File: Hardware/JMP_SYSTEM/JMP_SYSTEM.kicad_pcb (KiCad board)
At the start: 2 copper layers, 211.7 x 145 mm, 72 parts, among them J1 BLUEPILL, J10 Debug, J11 Debug, J12 RELE, J13 Port_access, J14 Port_access, J15 Port_access, J16 Port_access, J17 Port_access, J18 Port_access, J19 Port_access, J2 Debug, J20 Port_access, J21 Port_access, J22 Debug, J3 Debug, J4 BLUETOOTH, J5 MODULO SD, J6 Debug, J7 Debug, J8 Port_access, J9 Debug, SW1 SENSOR, SW10 BT_RST, SW2 SENSOR, SW3 BT_LEFT, SW4 BT_RIGHT, SW5 BT_UP, SW6 BT_DOWN, SW7 BT_STOP, SW8 BT_MENU, SW9 BT_OK, U1 LCD-PCF8574, U2 LCD-5LC02, U3 TP4056_MODULE, U4 Modulo_DC-DC_Boost_XL6009

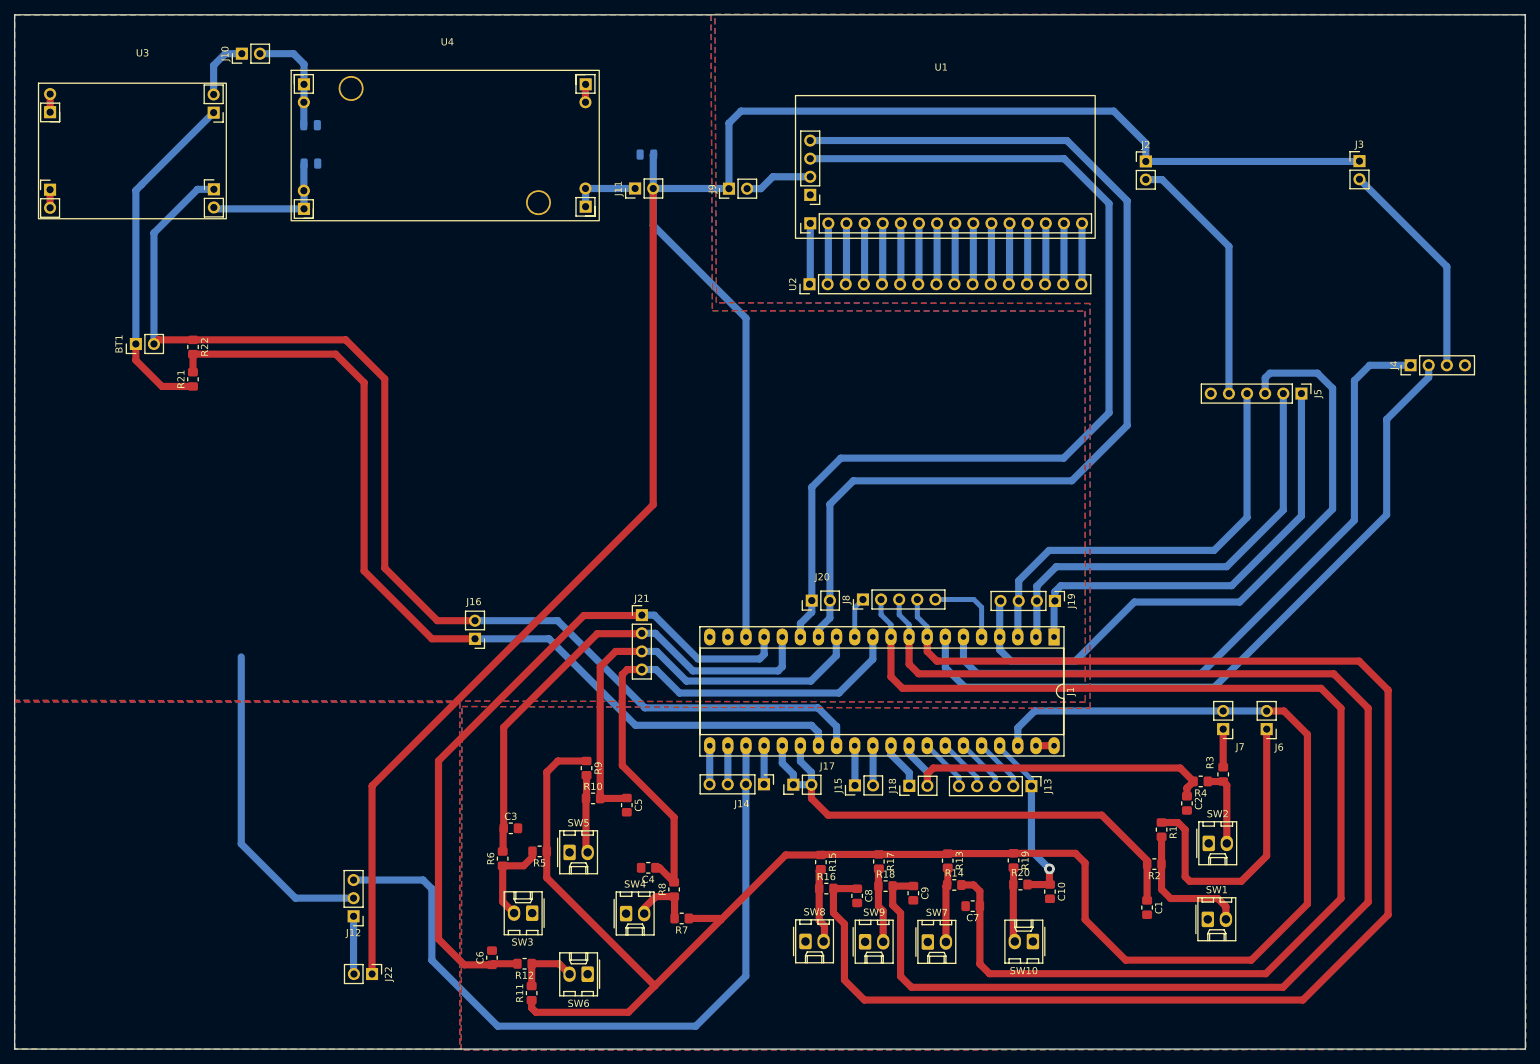
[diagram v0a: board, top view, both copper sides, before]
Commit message: Separacao do projeto em 3 PCBs - Core, PowerSupply, Display
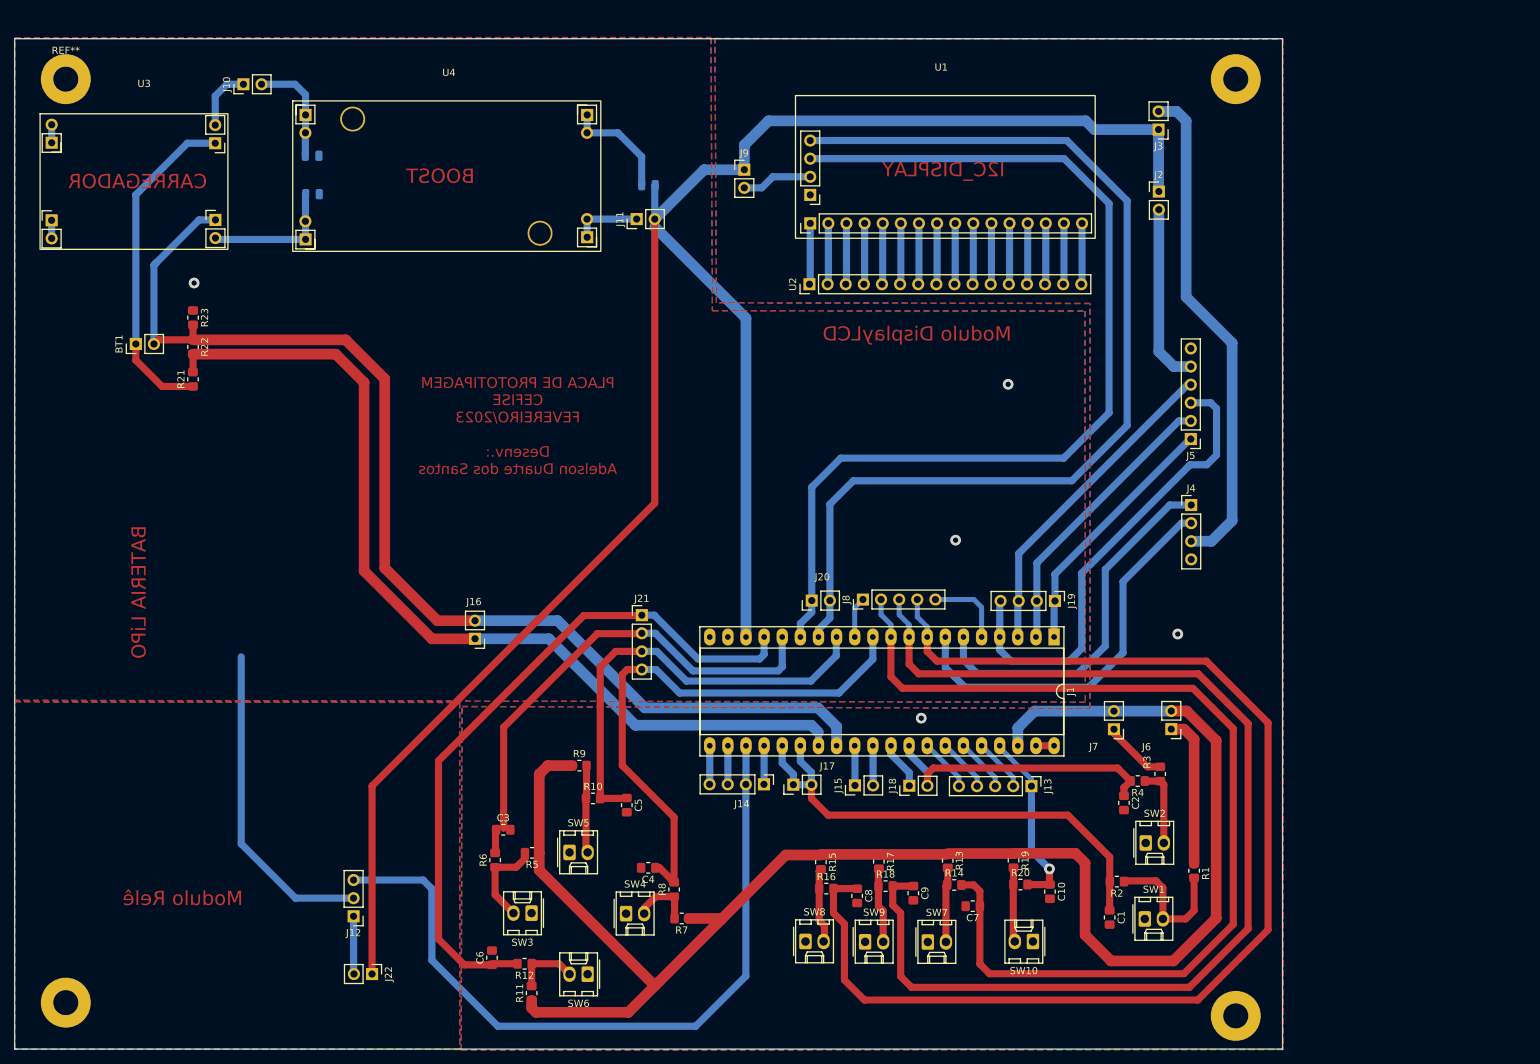
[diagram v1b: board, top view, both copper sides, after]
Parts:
- added ?: , , F.Cu at (-239.8, 155.3)
- added ?: , , F.Cu at (-72.7, 157.1)
- added ?: , , F.Cu at (-74.3, 25.5)
- added R23: R0, Resistor_SMD:R_0805_2012Metric_Pad1.20x1.40mm_HandSolder, F.Cu at (-220.4, 59.3)
- added REF**: MountingHole_3mm_Pad, MountingHole:MountingHole_3mm_Pad, F.Cu at (-238.3, 25.9)
- C12: value 1uF -> R0
- moved J4 36.5 mm to (-80.5, 85.5), turned to 0 degrees
- moved J3 28.5 mm to (-85.1, 32.9), turned to 180 degrees
- moved J5 16.8 mm to (-80.6, 76.3), turned to 180 degrees
- moved J7 15.3 mm to (-91.3, 117.0)
- moved J6 13.4 mm to (-83.3, 117.0)
- moved C2 8.83 mm to (-89.9, 127.3)
- moved R3 8.83 mm to (-84.9, 123.2)
- moved R4 8.83 mm to (-88.0, 124.2)
- moved SW1 8.83 mm to (-87.0, 143.6)
- moved SW2 8.83 mm to (-86.9, 132.9)
- moved R1 7.34 mm to (-80.1, 136.8)
- moved R2 5.79 mm to (-90.9, 138.3)
- moved C1 5.43 mm to (-91.9, 143.4)
- moved J2 4.60 mm to (-85.0, 41.6)
- moved C11 4.29 mm to (-203.7, 36.6)
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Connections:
- net Net-(J10-Pad1) renamed /PowerManagaement/4.2V
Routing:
- net /TX: track 100.7 -> 55.3 mm
- net /RX: track 96.0 -> 52.0 mm
- net Net-(J3-Pad2): track 31.1 -> 70.1 mm
- net /BT_MENU: track 205.3 -> 170.2 mm
- net 5V: track 312.8 -> 278.4 mm
- net /BT_OK: track 190.8 -> 158.1 mm
- net /BT_STOP: track 171.7 -> 141.9 mm
- net /CS: track 62.5 -> 35.7 mm
- net /MOSI: track 92.8 -> 66.6 mm
- net 3V3: track 249.6 -> 225.2 mm
- net /SCK: track 62.5 -> 40.3 mm
- net Net-(J6-Pad1): track 41.3 -> 21.2 mm
- net /MISO: track 61.0 -> 45.7 mm
- net GNDA: track 58.7 -> 71.8 mm, vias 0 -> 5
- net Net-(J2-Pad2): track 36.2 -> 25.2 mm
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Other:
- board size 211.7 x 145 mm -> 177.7 x 141.6 mm
- board text added: "BOOST"
- board text added: "CARREGADOR"
- board text added: "I2C_DISPLAY"
- board text added: "PLACA DE PROTOTIPAGEM CEFISE FEVEREIRO/2023 Desenv.: Adelson Duarte dos Santos"
- board text removed: "Modulo Bluetooth"
- board text removed: "Modulo MicroSD"

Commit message: Roteamento considerando I2C e Display em conjunto. O display ficara suspenso. Adicionado molex em todos os conectores. Debugs sao pinos convencionais
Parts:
- removed ? (x3): , 
- removed BT1: 4.2V, Connector_PinHeader_2.54mm:PinHeader_1x02_P2.54mm_Vertical
- removed C12: R0, Capacitor_SMD:C_0805_2012Metric
- removed J15: Port_access, Connector_PinHeader_2.54mm:PinHeader_1x02_P2.54mm_Vertical
- removed REF**: MountingHole_3mm_Pad, MountingHole:MountingHole_3mm_Pad
- removed U1: LCD-PCF8574, adelson:Módulo I2C - PCF8574
- removed U2: LCD-5LC02, Connector_PinHeader_2.54mm:PinHeader_1x16_P2.54mm_Vertical
- added Bateria1: 4.2V, Connector_Molex:Molex_KK-254_AE-6410-02A_1x02_P2.54mm_Vertical, F.Cu at (89.8, 66.0)
- added D1: 1N4148, Diode_SMD:D_MiniMELF_Handsoldering, F.Cu at (89.2, 129.8)
- added D2: LED, Connector_Molex:Molex_KK-254_AE-6410-02A_1x02_P2.54mm_Vertical, F.Cu at (134.9, 152.7)
- added D3: LED, Connector_Molex:Molex_KK-254_AE-6410-02A_1x02_P2.54mm_Vertical, F.Cu at (141.9, 152.7)
- added D4: LED, Connector_Molex:Molex_KK-254_AE-6410-02A_1x02_P2.54mm_Vertical, F.Cu at (151.4, 152.7)
- added J23: Debug, Connector_PinHeader_2.54mm:PinHeader_1x02_P2.54mm_Vertical, F.Cu at (199.6, 135.6)
- added J24: Display I/O Interface, Connector_Molex:Molex_KK-254_AE-6410-04A_1x04_P2.54mm_Vertical, F.Cu at (146.9, 63.1)
- added K1: FINDER-36.11, Relay_THT:Relay_SPDT_Finder_36.11, F.Cu at (89.2, 133.6)
- added Q1: MMBT2222A, Package_TO_SOT_SMD:SOT-23, F.Cu at (86.0, 153.9)
- added R24: 2.2k, Resistor_SMD:R_1206_3216Metric_Pad1.30x1.75mm_HandSolder, F.Cu at (92.3, 154.3)
- added R25: 1k, Resistor_SMD:R_0805_2012Metric_Pad1.20x1.40mm_HandSolder, F.Cu at (150.7, 131.1)
- added R26: 1k, Resistor_SMD:R_0805_2012Metric_Pad1.20x1.40mm_HandSolder, F.Cu at (160.3, 130.4)
- added R27: 1k, Resistor_SMD:R_0805_2012Metric_Pad1.20x1.40mm_HandSolder, F.Cu at (164.1, 130.4)
- C11, C13: moved to F.Cu
- J12: value RELE -> Buzzer; footprint Connector_PinHeader_2.54mm:PinHeader_1x03_P2.54mm_Vertical -> Connector_Molex:Molex_KK-254_AE-6410-02A_1x02_P2.54mm_Vertical
- J13: value Port_access -> Ports; footprint Connector_PinHeader_2.54mm:PinHeader_1x05_P2.54mm_Vertical -> Connector_Molex:Molex_KK-254_AE-6410-05A_1x05_P2.54mm_Vertical
- J14: value Port_access -> Ports; footprint Connector_PinHeader_2.54mm:PinHeader_1x04_P2.54mm_Vertical -> Connector_Molex:Molex_KK-254_AE-6410-03A_1x03_P2.54mm_Vertical
- J16, J17, J18, J20: value Port_access -> Ports; footprint Connector_PinHeader_2.54mm:PinHeader_1x02_P2.54mm_Vertical -> Connector_Molex:Molex_KK-254_AE-6410-02A_1x02_P2.54mm_Vertical
- J19: value Port_access -> Ports; footprint Connector_PinHeader_2.54mm:PinHeader_1x04_P2.54mm_Vertical -> Connector_Molex:Molex_KK-254_AE-6410-05A_1x05_P2.54mm_Vertical
- J21: value Port_access -> Ports; footprint Connector_PinHeader_2.54mm:PinHeader_1x04_P2.54mm_Vertical -> Connector_Molex:Molex_KK-254_AE-6410-04A_1x04_P2.54mm_Vertical
- J4: footprint Connector_PinHeader_2.54mm:PinHeader_1x04_P2.54mm_Vertical -> Connector_Molex:Molex_KK-254_AE-6410-04A_1x04_P2.54mm_Vertical
- J5: footprint Connector_PinHeader_2.54mm:PinHeader_1x06_P2.54mm_Vertical -> Connector_Molex:Molex_KK-254_AE-6410-06A_1x06_P2.54mm_Vertical
- J8: value Port_access -> Ports; footprint Connector_PinHeader_2.54mm:PinHeader_1x05_P2.54mm_Vertical -> Connector_Molex:Molex_KK-254_AE-6410-04A_1x04_P2.54mm_Vertical
- moved J9 359.7 mm to (199.6, 147.6), turned to 180 degrees
- moved J16 317.0 mm to (135.5, 124.1), turned to 90 degrees
- moved R22 316.1 mm to (95.6, 67.3), turned to 90 degrees
- moved R21 316.0 mm to (95.5, 61.3), turned to -90 degrees
- moved U3 309.2 mm to (66.7, 58.0), turned to -90 degrees
- moved R23 305.9 mm to (85.5, 60.3)
- moved J12 299.8 mm to (101.8, 146.9), turned to -90 degrees
- moved R11 297.1 mm to (124.1, 146.3), turned to 180 degrees
- moved R2 294.3 mm to (203.4, 139.6)
- moved SW1 293.7 mm to (206.6, 147.6), turned to 90 degrees
- moved SW2 293.6 mm to (206.6, 135.5), turned to 90 degrees
- moved J21 293.2 mm to (135.5, 110.1), turned to -90 degrees
- moved J8 291.9 mm to (165.4, 103.8), turned to 0 degrees
- moved C7 291.8 mm to (180.6, 149.7), turned to -90 degrees
- moved SW3 290.7 mm to (117.7, 144.3)
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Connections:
- J1 pad 1: /CS -> /PB12
- J1 pad 24: /PC15 -> /LED_3
- J1 pad 27: /B+_AD_IN -> /B-_AD_IN
- J1 pad 28: /B-_AD_IN -> /B+_AD_IN
- J1 pad 29: /PA4 -> /LED_2
- J1 pad 30: /PA5 -> /LED_1
- J1 pad 5: /PA8 -> /CS
- J12 pad 1: Net-(J12-Pad1) -> /User _IO/COM1
- J13 pad 1: /BT_RST -> /PB0
- J13 pad 2: /PB11 -> /PB1
- J13 pad 4: /PB1 -> /PB11
- J13 pad 5: /PB0 -> /BT_RST
- J14 pad 1: /PC15 -> /VBAT
- J14 pad 2: /RELE -> /PC13
- J14 pad 3: /PC13 -> /RELE
- J16 pad 1: /B+_AD_IN -> /B-_AD_IN
- J16 pad 2: /B-_AD_IN -> /B+_AD_IN
- J19 pad 1: /CS -> /PB12
- J22 pad 2: Net-(J12-Pad1) -> Net-(J22-Pad2)
- J4 pad 1: /RX -> GNDA
- J4 pad 2: /TX -> Net-(J3-Pad2)
- J4 pad 3: Net-(J3-Pad2) -> /TX
- J4 pad 4: GNDA -> /RX
- J9 pad 1: 5V -> GNDA
- J9 pad 2: Net-(J9-Pad2) -> Net-(R1-Pad2)
- U3 pad 5: Net-(U3-Pad5) -> GNDA
- U4 pad 2: Net-(U3-Pad5) -> GNDA
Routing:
- net /SCL: track 144.9 -> 52.0 mm
- net /SDA: track 141.5 -> 52.0 mm
- net GNDA: track 71.8 -> 2.54 mm, vias 5 -> 1
- net Net-(J3-Pad2): track 70.1 -> 10.3 mm
- net 5V: track 278.4 -> 221.4 mm, vias 0 -> 5
- net 3V3: track 225.2 -> 176.3 mm, vias 0 -> 2
- net /TX: track 55.3 -> 91.0 mm, vias 0 -> 1
- net /MOSI: track 66.6 -> 31.4 mm
- net /RX: track 52.0 -> 84.9 mm
- net /User _IO/V-K2: track 0.00 -> 31.0 mm
- net Net-(D4-Pad2): track 0.00 -> 30.5 mm, vias 0 -> 1
- net Net-(D3-Pad2): track 0.00 -> 29.7 mm, vias 0 -> 1
- net /User _IO/COM1: track 0.00 -> 27.7 mm
- net /RELE: track 104.7 -> 78.0 mm, vias 0 -> 1
- net Net-(D2-Pad2): track 0.00 -> 26.1 mm, vias 0 -> 1
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- removed copper zone on B.Cu, net GNDA
- removed copper zone on F.Cu, net GNDA
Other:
- board size 177.7 x 141.6 mm -> 176.4 x 109.3 mm
- board text added: "+ -"
- board text added: "Bluetooth"
- board text added: "Modulo SD"
- board text removed: "I O"
- board text removed: "I2C_DISPLAY"
- board text removed: "Modulo DisplayLCD"
- board text removed: "Modulo Relê"
